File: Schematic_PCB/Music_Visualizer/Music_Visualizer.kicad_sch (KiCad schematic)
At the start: 130 parts, among them J1 AudioJack2_Ground, U1 LM324, U2 LM324, U3 LM324, U4 LM324, U5 LM324, U6 LM324

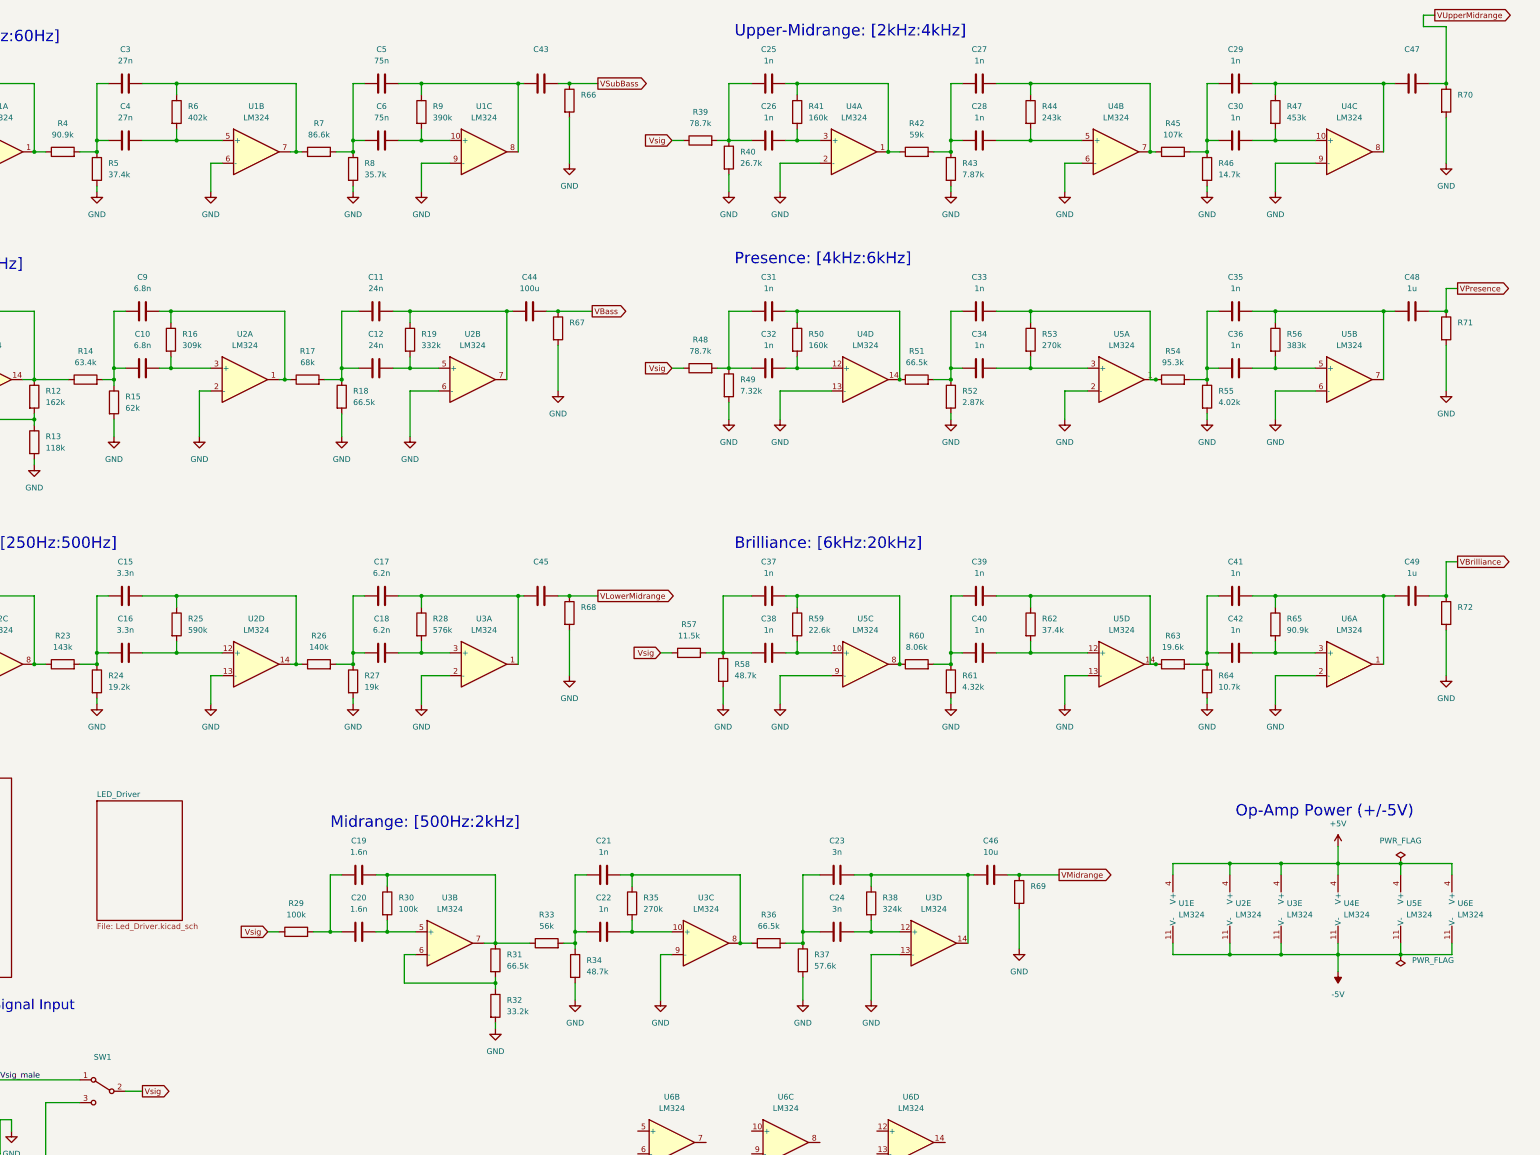
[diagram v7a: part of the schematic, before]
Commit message: Sourced on_off switch and added on_off switch/indicator circuit
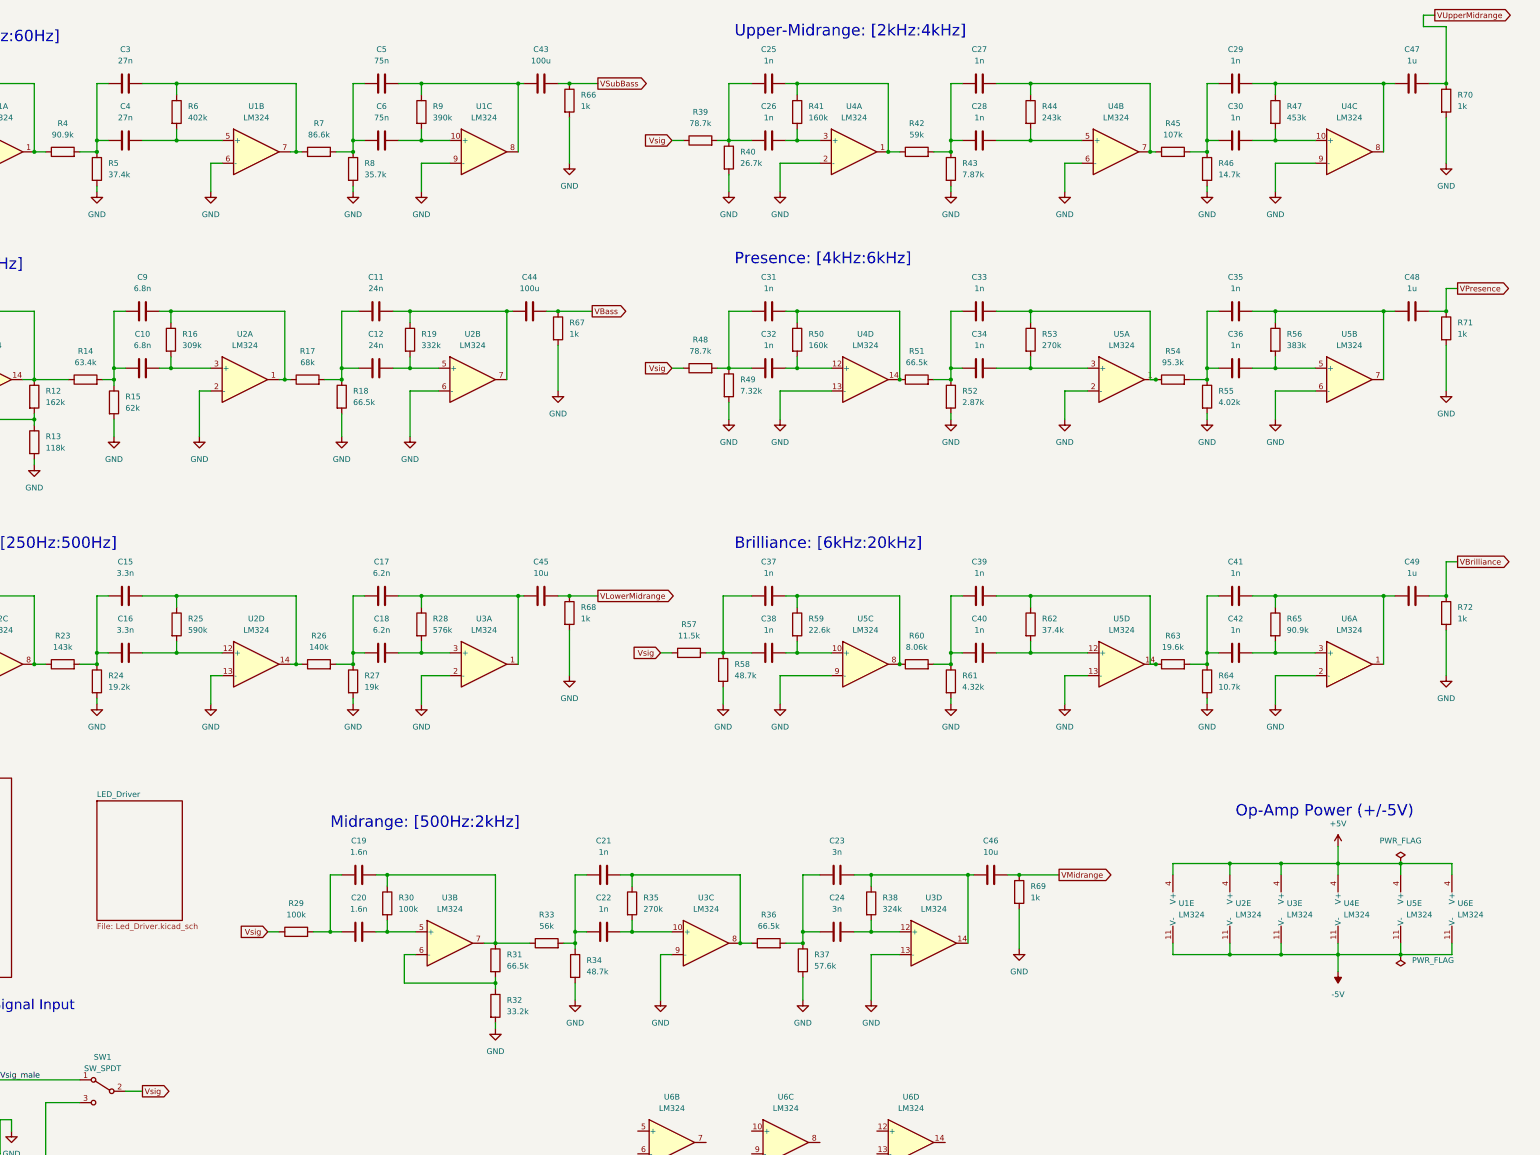
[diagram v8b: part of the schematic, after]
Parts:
- C43: value (none) -> 100u; footprint (none) -> Capacitor_SMD:C_1206_3216Metric
- C45: value (none) -> 10u; footprint (none) -> Capacitor_SMD:C_0805_2012Metric
- C47: value (none) -> 1u; footprint (none) -> Capacitor_SMD:C_0402_1005Metric
- R66, R67, R68, R69, R70, R71, R72: value (none) -> 1k; footprint (none) -> Resistor_SMD:R_0201_0603Metric
- SW1: value (none) -> SW_SPDT; footprint (none) -> Slide_Switch:SW_OS102011MS2QN1
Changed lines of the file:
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@@
       (effects (font (size 1.27 1.27)) (justify left))
     )
-    (property "Value" "" (id 1) (at 198.12 153.67 0)
+    (property "Value" "1k" (id 1) (at 198.12 153.67 0)
       (effects (font (size 1.27 1.27)) (justify left))
     )
-    (property "Footprint" "" (id 2) (at 193.802 152.4 90)
+    (property "Footprint" "Resistor_SMD:R_0201_0603Metric" (id 2) (at 193.802 152.4 90)
       (effects (font (size 1.27 1.27)) hide)
     )
@@
     (in_bom yes) (on_board yes) (fields_autoplaced)
     (property "Reference" "C43" (id 0) (at 189.23 26.67 90))
-    (property "Value" "" (id 1) (at 189.23 29.21 90))
-    (property "Footprint" "" (id 2) (at 193.04 33.3248 0)
+    (property "Value" "100u" (id 1) (at 189.23 29.21 90))
+    (property "Footprint" "Capacitor_SMD:C_1206_3216Metric" (id 2) (at 193.04 33.3248 0)
       (effects (font (size 1.27 1.27)) hide)
     )
@@
     (in_bom yes) (on_board yes) (fields_autoplaced)
     (property "Reference" "C47" (id 0) (at 383.54 26.67 90))
-    (property "Value" "" (id 1) (at 383.54 29.21 90))
-    (property "Footprint" "" (id 2) (at 387.35 33.3248 0)
+    (property "Value" "1u" (id 1) (at 383.54 29.21 90))
+    (property "Footprint" "Capacitor_SMD:C_0402_1005Metric" (id 2) (at 387.35 33.3248 0)
       (effects (font (size 1.27 1.27)) hide)
     )
@@
       (effects (font (size 1.27 1.27)) (justify left))
     )
-    (property "Value" "" (id 1) (at 298.45 215.8999 0)
+    (property "Value" "1k" (id 1) (at 298.45 215.8999 0)
       (effects (font (size 1.27 1.27)) (justify left))
     )
-    (property "Footprint" "" (id 2) (at 294.132 214.63 90)
+    (property "Footprint" "Resistor_SMD:R_0201_0603Metric" (id 2) (at 294.132 214.63 90)
       (effects (font (size 1.27 1.27)) hide)
     )
@@
       (effects (font (size 1.27 1.27)) (justify left))
     )
-    (property "Value" "" (id 1) (at 393.7 39.3699 0)
+    (property "Value" "1k" (id 1) (at 393.7 39.3699 0)
       (effects (font (size 1.27 1.27)) (justify left))
     )
-    (property "Footprint" "" (id 2) (at 389.382 38.1 90)
+    (property "Footprint" "Resistor_SMD:R_0201_0603Metric" (id 2) (at 389.382 38.1 90)
       (effects (font (size 1.27 1.27)) hide)
     )
@@
       (effects (font (size 1.27 1.27)) (justify left))
     )
-    (property "Value" "" (id 1) (at 393.7 153.6699 0)
+    (property "Value" "1k" (id 1) (at 393.7 153.6699 0)
       (effects (font (size 1.27 1.27)) (justify left))
     )
-    (property "Footprint" "" (id 2) (at 389.382 152.4 90)
+    (property "Footprint" "Resistor_SMD:R_0201_0603Metric" (id 2) (at 389.382 152.4 90)
       (effects (font (size 1.27 1.27)) hide)
     )
@@
       (effects (font (size 1.27 1.27)) (justify left))
     )
-    (property "Value" "" (id 1) (at 198.12 39.3699 0)
+    (property "Value" "1k" (id 1) (at 198.12 39.3699 0)
       (effects (font (size 1.27 1.27)) (justify left))
     )
-    (property "Footprint" "" (id 2) (at 193.802 38.1 90)
+    (property "Footprint" "Resistor_SMD:R_0201_0603Metric" (id 2) (at 193.802 38.1 90)
       (effects (font (size 1.27 1.27)) hide)
     )
@@
       (effects (font (size 1.27 1.27)) (justify left))
     )
-    (property "Value" "" (id 1) (at 195.58 90.1699 0)
+    (property "Value" "1k" (id 1) (at 195.58 90.1699 0)
       (effects (font (size 1.27 1.27)) (justify left))
     )
-    (property "Footprint" "" (id 2) (at 191.262 88.9 90)
+    (property "Footprint" "Resistor_SMD:R_0201_0603Metric" (id 2) (at 191.262 88.9 90)
       (effects (font (size 1.27 1.27)) hide)
     )
@@
     (in_bom yes) (on_board yes) (fields_autoplaced)
     (property "Reference" "C45" (id 0) (at 189.23 140.97 90))
-    (property "Value" "" (id 1) (at 189.23 143.51 90))
-    (property "Footprint" "" (id 2) (at 193.04 147.6248 0)
+    (property "Value" "10u" (id 1) (at 189.23 143.51 90))
+    (property "Footprint" "Capacitor_SMD:C_0805_2012Metric" (id 2) (at 193.04 147.6248 0)
       (effects (font (size 1.27 1.27)) hide)
     )
@@
       (effects (font (size 1.27 1.27)) (justify left))
     )
-    (property "Value" "" (id 1) (at 393.7 90.1699 0)
+    (property "Value" "1k" (id 1) (at 393.7 90.1699 0)
       (effects (font (size 1.27 1.27)) (justify left))
     )
-    (property "Footprint" "" (id 2) (at 389.382 88.9 90)
+    (property "Footprint" "Resistor_SMD:R_0201_0603Metric" (id 2) (at 389.382 88.9 90)
       (effects (font (size 1.27 1.27)) hide)
     )
@@
     (in_bom yes) (on_board yes) (fields_autoplaced)
     (property "Reference" "SW1" (id 0) (at 91.44 251.46 0))
-    (property "Value" "" (id 1) (at 91.44 254 0))
-    (property "Footprint" "" (id 2) (at 91.44 259.08 0)
+    (property "Value" "SW_SPDT" (id 1) (at 91.44 254 0))
+    (property "Footprint" "Slide_Switch:SW_OS102011MS2QN1" (id 2) (at 91.44 259.08 0)
       (effects (font (size 1.27 1.27)) hide)
     )
@@
       (reference "#PWR089") (unit 1) (value "-5V") (footprint "")
     )
-    (path "/b067b2c9-ed79-4b19-b934-2a655714ed3e"
-      (reference "#PWR0101") (unit 1) (value "GND") (footprint "")
+    (path "/d77592bc-5812-4255-9ac4-28fcc93efec5/d84d37a6-1e20-4768-83ef-715822ba1176"
+      (reference "#PWR090") (unit 1) (value "GND") (footprint "")
+    )
+    (path "/56ed3a67-eed8-4688-8767-d6bf63bd87ca/f9251750-1ec8-4b28-94a2-e2c2fd034a76"
+      (reference "#PWR091") (unit 1) (value "GND") (footprint "")
     )
     (path "/56ed3a67-eed8-4688-8767-d6bf63bd87ca/a2358d1e-6b27-4973-acba-fcd63cd710b2"
-      (reference "#PWR?") (unit 1) (value "GND") (footprint "")
+      (reference "#PWR092") (unit 1) (value "GND") (footprint "")
     )
-    (path "/56ed3a67-eed8-4688-8767-d6bf63bd87ca/f9251750-1ec8-4b28-94a2-e2c2fd034a76"
-      (reference "#PWR?") (unit 1) (value "GND") (footprint "")
+    (path "/b067b2c9-ed79-4b19-b934-2a655714ed3e"
+      (reference "#PWR0101") (unit 1) (value "GND") (footprint "")
     )
     (path "/d3791e18-fb94-4a94-9f9d-30d4fd98db8e"
@@
       (reference "D70") (unit 1) (value "LED") (footprint "LED_THT:LED_D5.0mm")
     )
+    (path "/d77592bc-5812-4255-9ac4-28fcc93efec5/3d55304b-a0d7-4113-8774-ec8aae0193ab"
+      (reference "D71") (unit 1) (value "LED") (footprint "")
+    )
     (path "/5fded386-4830-4c6d-a6ca-3b530b67ab9c"
       (reference "J1") (unit 1) (value "AudioJack2_Ground") (footprint "Connector_Audio:Jack_3.5mm_CUI_SJ-3523-SMT_Horizontal")
@@
       (reference "R81") (unit 1) (value "680") (footprint "Resistor_SMD:R_0603_1608Metric")
     )
+    (path "/d77592bc-5812-4255-9ac4-28fcc93efec5/2e877dbb-6832-4630-bc2c-069ff902df6b"
+      (reference "R82") (unit 1) (value "330") (footprint "Resistor_SMD:R_0603_1608Metric")
+    )
     (path "/56ed3a67-eed8-4688-8767-d6bf63bd87ca/09eaa136-75d0-48fe-a03b-a1369df77003"
       (reference "RV1") (unit 1) (value "5k_LED_Brightness_Pot") (footprint "Potentiometer_THT:Potentiometer_Bourns_PTV09A-1_Single_Vertical")
@@
       (reference "SW1") (unit 1) (value "SW_SPDT") (footprint "Slide_Switch:SW_OS102011MS2QN1")
     )
+    (path "/d77592bc-5812-4255-9ac4-28fcc93efec5/05bdf75d-fbcd-400b-921d-ab6fd6737c47"
+      (reference "SW2") (unit 1) (value "SW_SPST") (footprint "PW_On_Off_Switch:E-SWITCH_RR511D1121")
+    )
     (path "/7a70fb5f-edf3-42ca-8da4-fb415c6f3b93"
